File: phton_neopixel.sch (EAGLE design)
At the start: 7 parts, among them J2 Neopixel, J3 POWER_JACK, U2 PHOTON_WITH_HEADERS

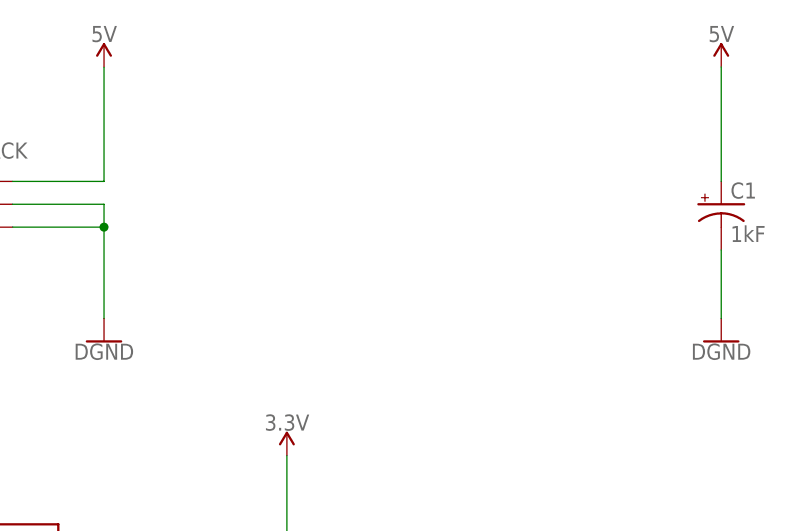
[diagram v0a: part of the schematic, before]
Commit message: Added filter caps and cleaned up the layout a lot
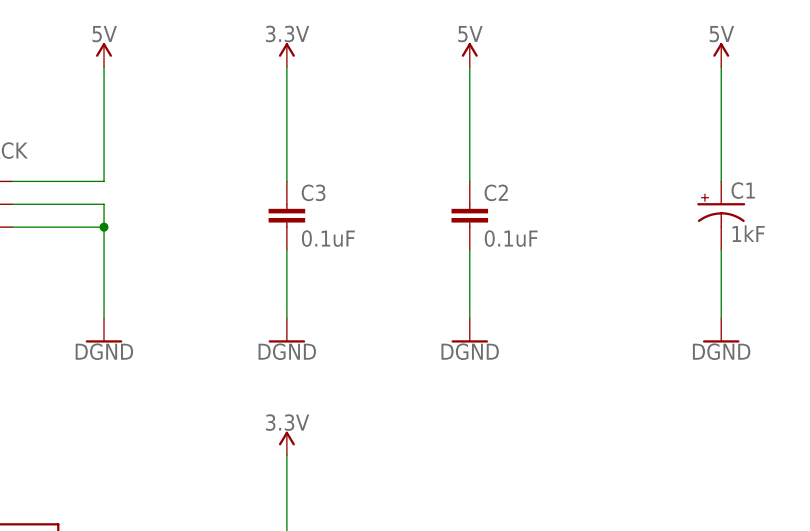
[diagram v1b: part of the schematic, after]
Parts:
- added C2, C3: 0.1uF, SparkFun-Capacitors:0.1UF-25V-5%(0603)
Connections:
- net 3.3V: now also C3.1
- net 5V: now also C2.1
- net GND: now also C2.2, C3.2
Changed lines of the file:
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@@
 <?xml version="1.0" encoding="utf-8"?>
 <!DOCTYPE eagle SYSTEM "eagle.dtd">
-<eagle version="7.6.0">
+<eagle version="7.4.0">
 <drawing>
 <settings>
@@
 <part name="SUPPLY6" library="SparkFun-PowerSymbols" deviceset="5V" device=""/>
 <part name="SUPPLY7" library="SparkFun-PowerSymbols" deviceset="3.3V" device=""/>
+<part name="C2" library="SparkFun-Capacitors" deviceset="0.1UF-25V-5%(0603)" device="" value="0.1uF"/>
+<part name="GND10" library="SparkFun-PowerSymbols" deviceset="DGND" device=""/>
+<part name="SUPPLY9" library="SparkFun-PowerSymbols" deviceset="5V" device=""/>
+<part name="C3" library="SparkFun-Capacitors" deviceset="0.1UF-25V-5%(0603)" device="" value="0.1uF"/>
+<part name="SUPPLY8" library="SparkFun-PowerSymbols" deviceset="3.3V" device=""/>
+<part name="GND9" library="SparkFun-PowerSymbols" deviceset="DGND" device=""/>
 </parts>
 <sheets>
@@
 <instance part="SUPPLY6" gate="G$1" x="-241.3" y="78.74"/>
 <instance part="SUPPLY7" gate="G$1" x="-172.72" y="78.74"/>
+<instance part="C2" gate="G$1" x="-152.4" y="104.14"/>
+<instance part="GND10" gate="G$1" x="-152.4" y="91.44"/>
+<instance part="SUPPLY9" gate="G$1" x="-152.4" y="121.92"/>
+<instance part="C3" gate="G$1" x="-172.72" y="104.14"/>
+<instance part="SUPPLY8" gate="G$1" x="-172.72" y="121.92"/>
+<instance part="GND9" gate="G$1" x="-172.72" y="91.44"/>
 </instances>
 <busses>
@@
 <junction x="-193.04" y="104.14"/>
 </segment>
+<segment>
+<pinref part="C2" gate="G$1" pin="2"/>
+<pinref part="GND10" gate="G$1" pin="GND"/>
+<wire x1="-152.4" y1="101.6" x2="-152.4" y2="93.98" width="0.1524" layer="91"/>
+</segment>
+<segment>
+<pinref part="GND9" gate="G$1" pin="GND"/>
+<pinref part="C3" gate="G$1" pin="2"/>
+<wire x1="-172.72" y1="93.98" x2="-172.72" y2="101.6" width="0.1524" layer="91"/>
+</segment>
 </net>
 <net name="3.3V" class="0">
@@
 <wire x1="-172.72" y1="66.04" x2="-172.72" y2="78.74" width="0.1524" layer="91"/>
 <pinref part="SUPPLY7" gate="G$1" pin="3.3V"/>
+</segment>
+<segment>
+<pinref part="C3" gate="G$1" pin="1"/>
+<pinref part="SUPPLY8" gate="G$1" pin="3.3V"/>
+<wire x1="-172.72" y1="109.22" x2="-172.72" y2="121.92" width="0.1524" layer="91"/>
 </segment>
 </net>
@@
 <wire x1="-241.3" y1="66.04" x2="-220.98" y2="66.04" width="0.1524" layer="91"/>
 </segment>
+<segment>
+<pinref part="SUPPLY9" gate="G$1" pin="5V"/>
+<pinref part="C2" gate="G$1" pin="1"/>
+<wire x1="-152.4" y1="121.92" x2="-152.4" y2="109.22" width="0.1524" layer="91"/>
+</segment>
 </net>

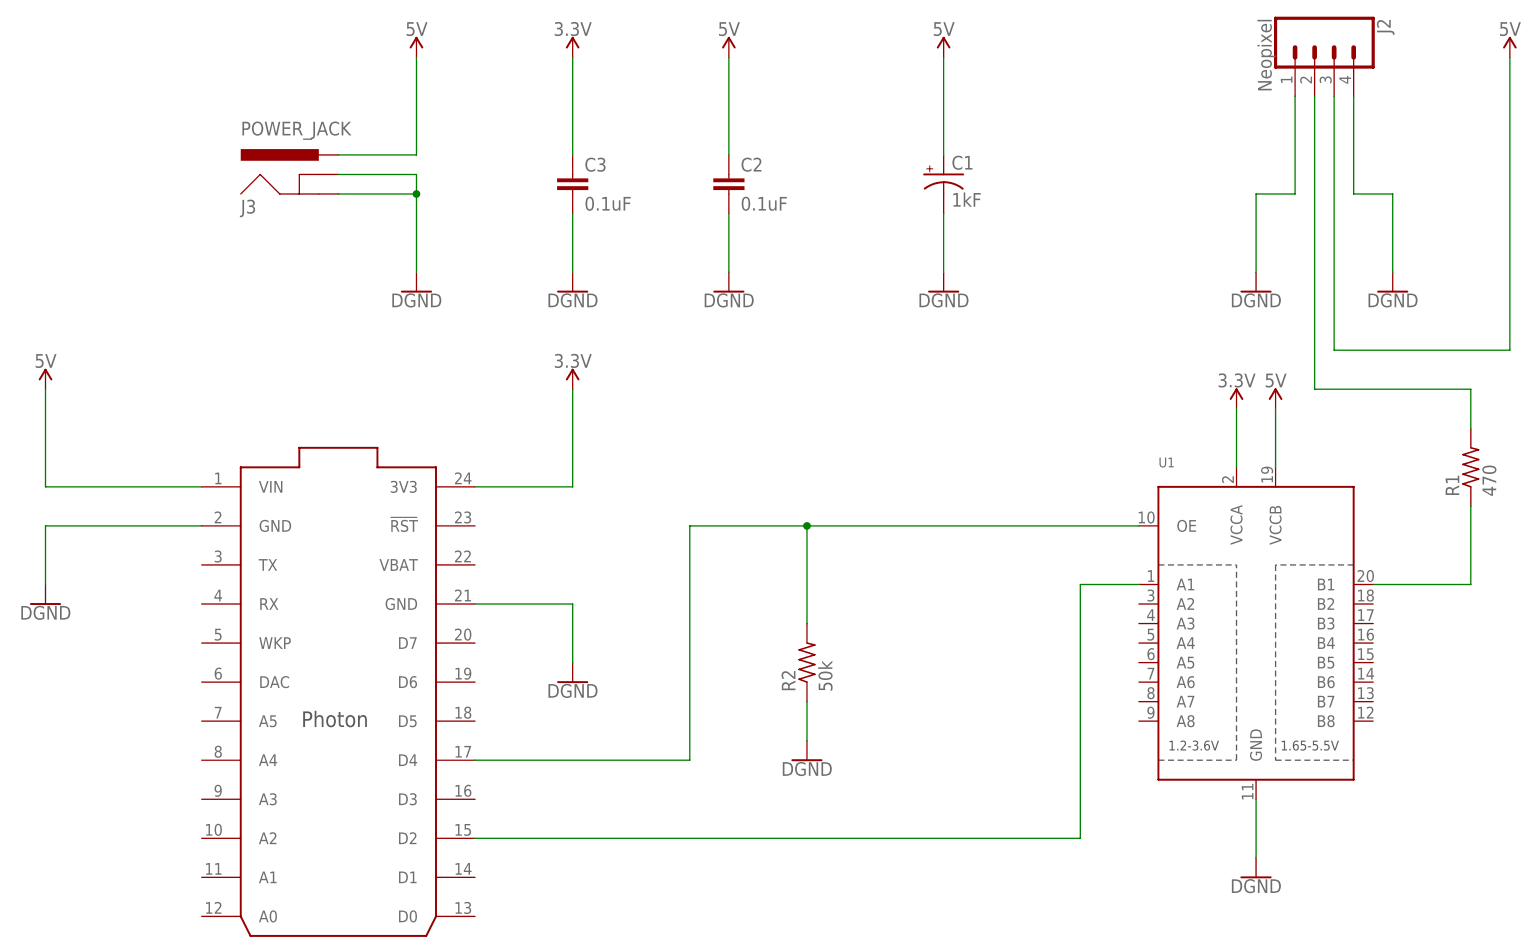
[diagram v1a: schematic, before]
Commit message: Added jumper for 5V to the photon, improved routing and naming
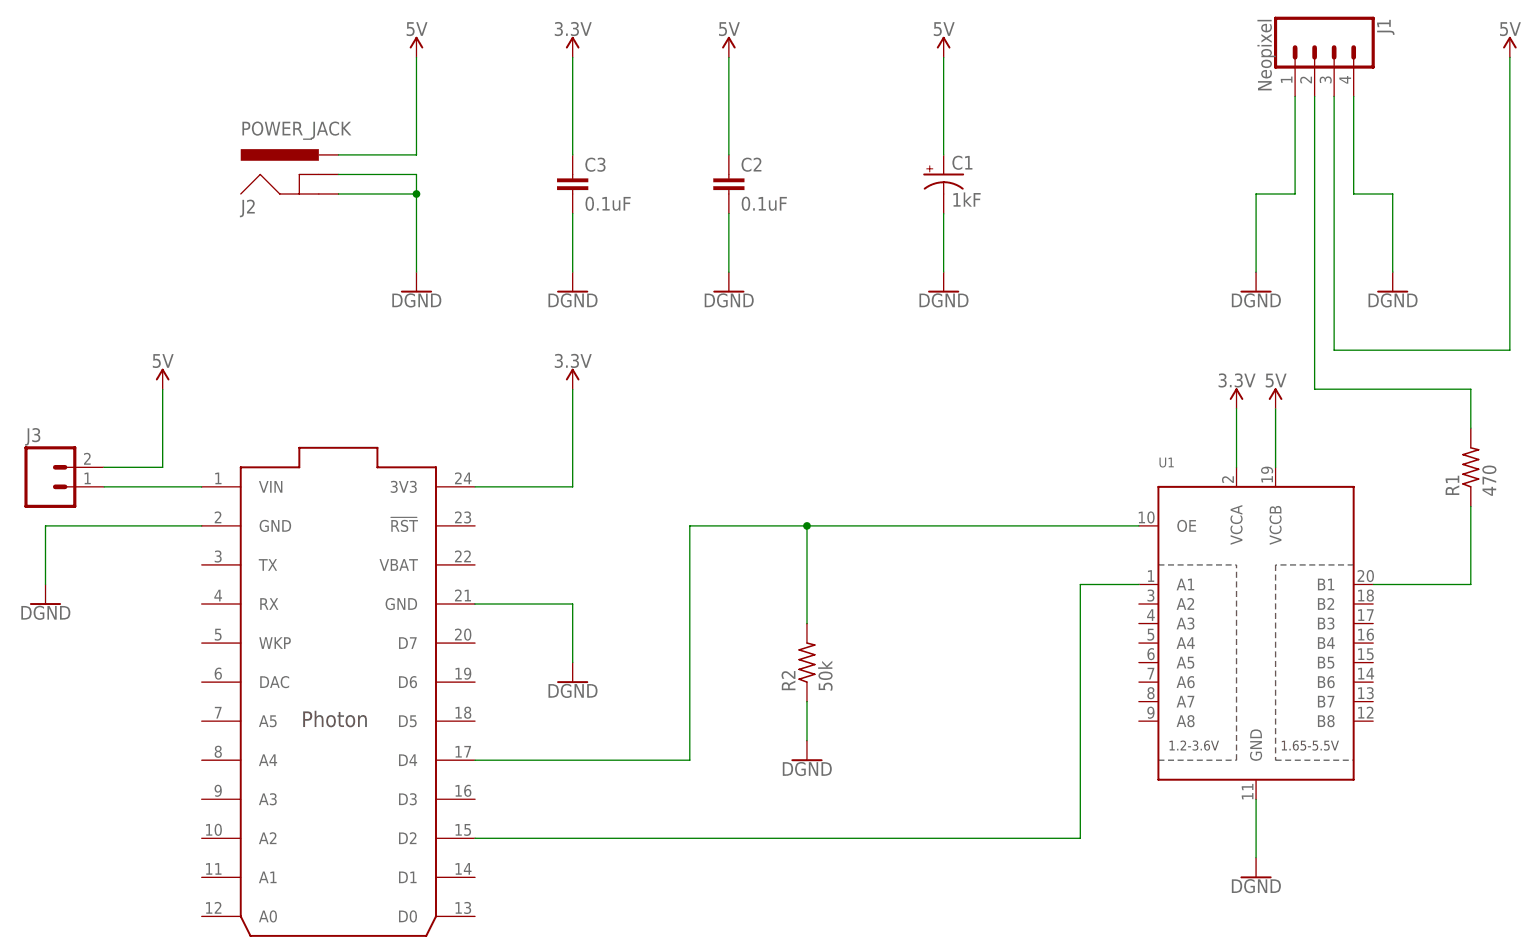
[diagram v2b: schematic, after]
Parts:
- added J1: Neopixel, SparkFun-Connectors:CONN_04
- J2: value Neopixel -> POWER_JACK; device SparkFun-Connectors:CONN_04 -> SparkFun-Connectors:POWER_JACK
- J3: value POWER_JACK -> (none); device SparkFun-Connectors:POWER_JACK -> SparkFun-Connectors:M02PTH
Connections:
- new net N$2: J3.1, U2.VIN
- net 5V: now also J1.3, J2.PWR, J3.2; no longer J2.3, J3.PWR, U2.VIN
- net GND: now also J1.1, J1.4, J2.GND, J2.GNDBREAK; no longer J2.1, J2.4, J3.GND, J3.GNDBREAK
- net N$4: now also J1.2; no longer J2.2
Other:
- moved on the sheet: J3
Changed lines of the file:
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@@
 <part name="R1" library="resistor" deviceset="R-US_" device="0207/7" value="470"/>
 <part name="R2" library="resistor" deviceset="R-US_" device="0207/7" value="50k"/>
-<part name="J2" library="SparkFun-Connectors" deviceset="CONN_04" device="" value="Neopixel"/>
+<part name="J1" library="SparkFun-Connectors" deviceset="CONN_04" device="" value="Neopixel"/>
 <part name="U1" library="adafruit" deviceset="TXB0108PWR" device=""/>
 <part name="GND1" library="SparkFun-PowerSymbols" deviceset="DGND" device=""/>
@@
 <part name="SUPPLY5" library="SparkFun-PowerSymbols" deviceset="5V" device=""/>
 <part name="GND8" library="SparkFun-PowerSymbols" deviceset="DGND" device=""/>
-<part name="J3" library="SparkFun-Connectors" deviceset="POWER_JACK" device=""/>
+<part name="J2" library="SparkFun-Connectors" deviceset="POWER_JACK" device=""/>
 <part name="SUPPLY6" library="SparkFun-PowerSymbols" deviceset="5V" device=""/>
 <part name="SUPPLY7" library="SparkFun-PowerSymbols" deviceset="3.3V" device=""/>
@@
 <part name="SUPPLY8" library="SparkFun-PowerSymbols" deviceset="3.3V" device=""/>
 <part name="GND9" library="SparkFun-PowerSymbols" deviceset="DGND" device=""/>
+<part name="J3" library="SparkFun-Connectors" deviceset="M02" device="PTH"/>
 </parts>
 <sheets>
@@
 <instance part="R1" gate="G$1" x="-55.88" y="68.58" rot="R90"/>
 <instance part="R2" gate="G$1" x="-142.24" y="43.18" rot="R90"/>
-<instance part="J2" gate="G$1" x="-76.2" y="121.92" rot="R270"/>
+<instance part="J1" gate="G$1" x="-76.2" y="121.92" rot="R270"/>
 <instance part="U1" gate="G$1" x="-83.82" y="48.26"/>
 <instance part="GND1" gate="G$1" x="-124.46" y="91.44"/>
@@
 <instance part="SUPPLY5" gate="G$1" x="-193.04" y="121.92"/>
 <instance part="GND8" gate="G$1" x="-142.24" y="30.48"/>
-<instance part="J3" gate="G$1" x="-205.74" y="101.6"/>
-<instance part="SUPPLY6" gate="G$1" x="-241.3" y="78.74"/>
+<instance part="J2" gate="G$1" x="-205.74" y="101.6"/>
+<instance part="SUPPLY6" gate="G$1" x="-226.06" y="78.74"/>
 <instance part="SUPPLY7" gate="G$1" x="-172.72" y="78.74"/>
 <instance part="C2" gate="G$1" x="-152.4" y="104.14"/>
@@
 <instance part="SUPPLY8" gate="G$1" x="-172.72" y="121.92"/>
 <instance part="GND9" gate="G$1" x="-172.72" y="91.44"/>
+<instance part="J3" gate="G$1" x="-241.3" y="66.04"/>
 </instances>
 <busses>
@@
 </segment>
 <segment>
-<pinref part="J2" gate="G$1" pin="1"/>
+<pinref part="J1" gate="G$1" pin="1"/>
 <wire x1="-78.74" y1="116.84" x2="-78.74" y2="104.14" width="0.1524" layer="91"/>
 <wire x1="-78.74" y1="104.14" x2="-83.82" y2="104.14" width="0.1524" layer="91"/>
@@
 </segment>
 <segment>
-<pinref part="J2" gate="G$1" pin="4"/>
+<pinref part="J1" gate="G$1" pin="4"/>
 <pinref part="GND7" gate="G$1" pin="GND"/>
 <wire x1="-71.12" y1="116.84" x2="-71.12" y2="104.14" width="0.1524" layer="91"/>
@@
 </segment>
 <segment>
-<pinref part="J3" gate="G$1" pin="GND"/>
+<pinref part="J2" gate="G$1" pin="GND"/>
 <pinref part="GND6" gate="G$1" pin="GND"/>
 <wire x1="-203.2" y1="104.14" x2="-193.04" y2="104.14" width="0.1524" layer="91"/>
 <wire x1="-193.04" y1="104.14" x2="-193.04" y2="93.98" width="0.1524" layer="91"/>
-<pinref part="J3" gate="G$1" pin="GNDBREAK"/>
+<pinref part="J2" gate="G$1" pin="GNDBREAK"/>
 <wire x1="-203.2" y1="106.68" x2="-193.04" y2="106.68" width="0.1524" layer="91"/>
 <wire x1="-193.04" y1="106.68" x2="-193.04" y2="104.14" width="0.1524" layer="91"/>
@@
 </segment>
 <segment>
-<pinref part="J2" gate="G$1" pin="3"/>
+<pinref part="J1" gate="G$1" pin="3"/>
 <wire x1="-73.66" y1="116.84" x2="-73.66" y2="83.82" width="0.1524" layer="91"/>
 <wire x1="-73.66" y1="83.82" x2="-50.8" y2="83.82" width="0.1524" layer="91"/>
@@
 <pinref part="SUPPLY5" gate="G$1" pin="5V"/>
 <wire x1="-193.04" y1="121.92" x2="-193.04" y2="109.22" width="0.1524" layer="91"/>
-<pinref part="J3" gate="G$1" pin="PWR"/>
+<pinref part="J2" gate="G$1" pin="PWR"/>
 <wire x1="-193.04" y1="109.22" x2="-203.2" y2="109.22" width="0.1524" layer="91"/>
-</segment>
-<segment>
-<pinref part="SUPPLY6" gate="G$1" pin="5V"/>
-<wire x1="-241.3" y1="78.74" x2="-241.3" y2="66.04" width="0.1524" layer="91"/>
-<pinref part="U2" gate="G$1" pin="VIN"/>
-<wire x1="-241.3" y1="66.04" x2="-220.98" y2="66.04" width="0.1524" layer="91"/>
 </segment>
 <segment>
@@
 <wire x1="-152.4" y1="121.92" x2="-152.4" y2="109.22" width="0.1524" layer="91"/>
 </segment>
+<segment>
+<pinref part="J3" gate="G$1" pin="2"/>
+<pinref part="SUPPLY6" gate="G$1" pin="5V"/>
+<wire x1="-233.68" y1="68.58" x2="-226.06" y2="68.58" width="0.1524" layer="91"/>
+<wire x1="-226.06" y1="68.58" x2="-226.06" y2="78.74" width="0.1524" layer="91"/>
+</segment>
 </net>
 <net name="N$4" class="0">
 <segment>
-<pinref part="J2" gate="G$1" pin="2"/>
+<pinref part="J1" gate="G$1" pin="2"/>
 <wire x1="-55.88" y1="78.74" x2="-76.2" y2="78.74" width="0.1524" layer="91"/>
 <wire x1="-76.2" y1="78.74" x2="-76.2" y2="116.84" width="0.1524" layer="91"/>
@@
 </segment>
 </net>
+<net name="N$2" class="0">
+<segment>
+<pinref part="J3" gate="G$1" pin="1"/>
+<pinref part="U2" gate="G$1" pin="VIN"/>
+<wire x1="-233.68" y1="66.04" x2="-220.98" y2="66.04" width="0.1524" layer="91"/>
+</segment>
+</net>

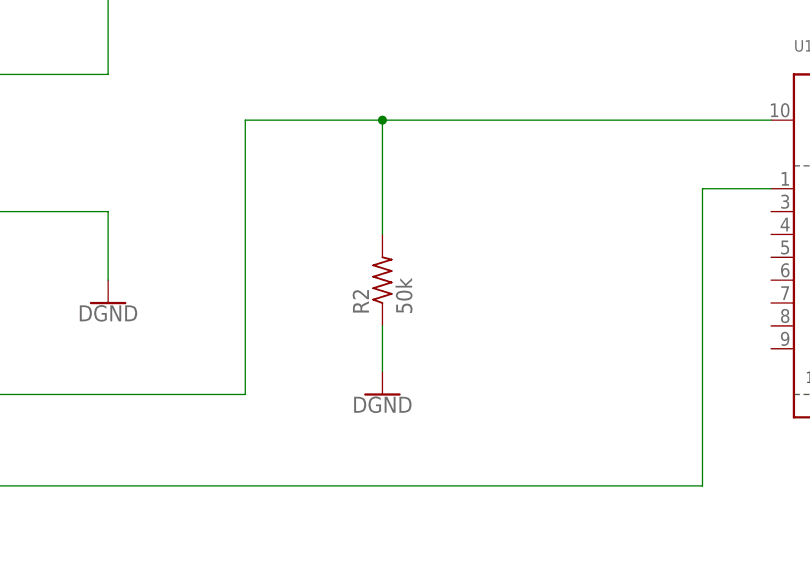
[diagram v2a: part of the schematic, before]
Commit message: Changed pull-down resistor to 100k
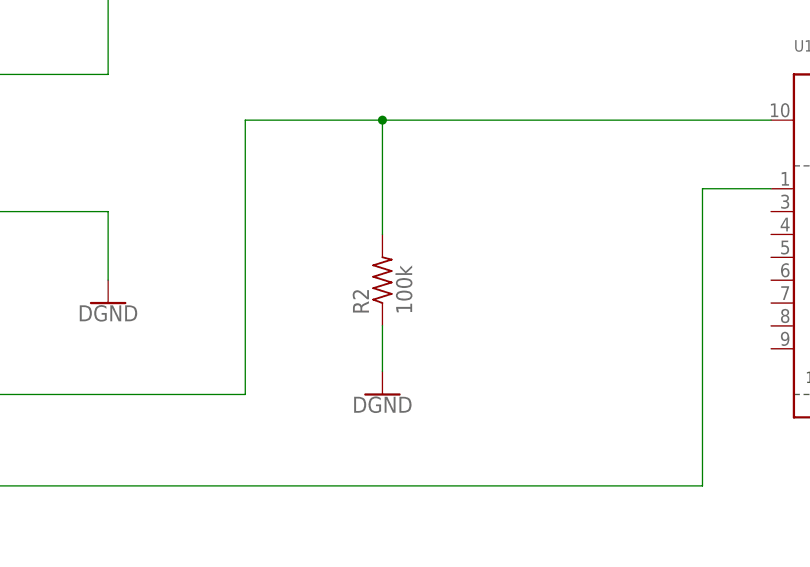
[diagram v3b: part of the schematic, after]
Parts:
- R2: value 50k -> 100k
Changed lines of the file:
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@@
 <part name="C1" library="SparkFun-Capacitors" deviceset="1000UF" device="-RADIAL-5MM-25V-20%" value="1kF"/>
 <part name="R1" library="resistor" deviceset="R-US_" device="0207/7" value="470"/>
-<part name="R2" library="resistor" deviceset="R-US_" device="0207/7" value="50k"/>
+<part name="R2" library="resistor" deviceset="R-US_" device="0207/7" value="100k"/>
 <part name="J1" library="SparkFun-Connectors" deviceset="CONN_04" device="" value="Neopixel"/>
 <part name="U1" library="adafruit" deviceset="TXB0108PWR" device=""/>
